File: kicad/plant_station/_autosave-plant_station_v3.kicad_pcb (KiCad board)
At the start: 2 copper layers, 73.4 x 43 mm, 89 parts, among them IC1 VEML7700-TT, IC3 TLC555CDR, IC4 ADC081C021CIMK_NOPB, J1 Conn_02x08_Odd_Even, J10 I2C HOST, J11 SOIL_I2C, J12 WEATHER_I2C, J13 ZF5S-20-01-T-WT-TR, J14 505567-0471, J15 505567-0471, J16 Conn_01x06, J17 Conn_01x08, J18 Conn_01x08, J19 Ammeter_Jumper, J2 MB_I2C, J3 MB_I2C, J4 ZF5S-20-01-T-WT-TR, J5 MB_I2C, J6 MB_I2C, J7 Conn_01x08, J8 Conn_01x06, J9 I2C SCREEN, P1 USB_C_Plug_USB2.0, Q1 DTC113Z, Q3 DTC113Z, Q4 DMG2301L, Q5 BC817DS,115, U1 HDC2010YPAT, U4 ESP-WROOM-02, U5 TPL5110, U6 CP2102N-A01-GQFN28

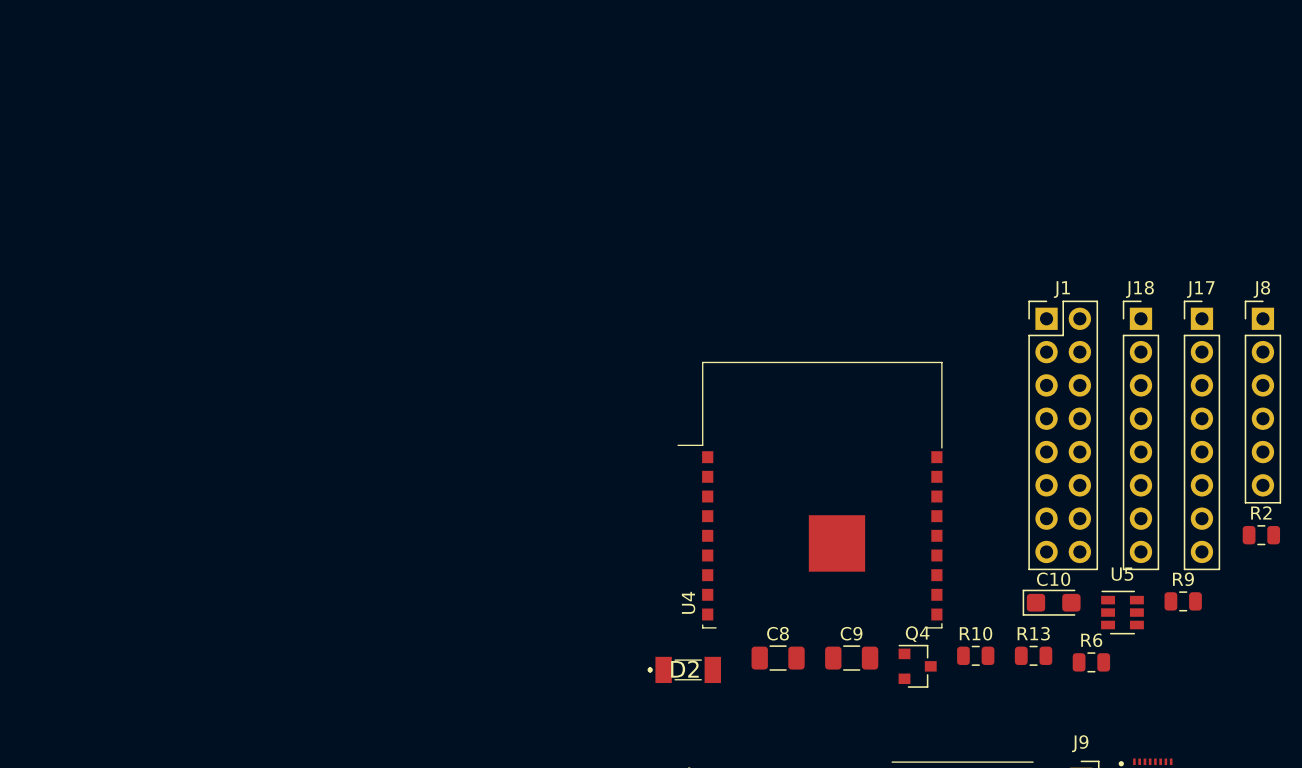
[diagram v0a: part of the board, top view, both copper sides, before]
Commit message: v3 PCB in progress. Need to move LED driver to LEDs board and make it connect using the standard interface
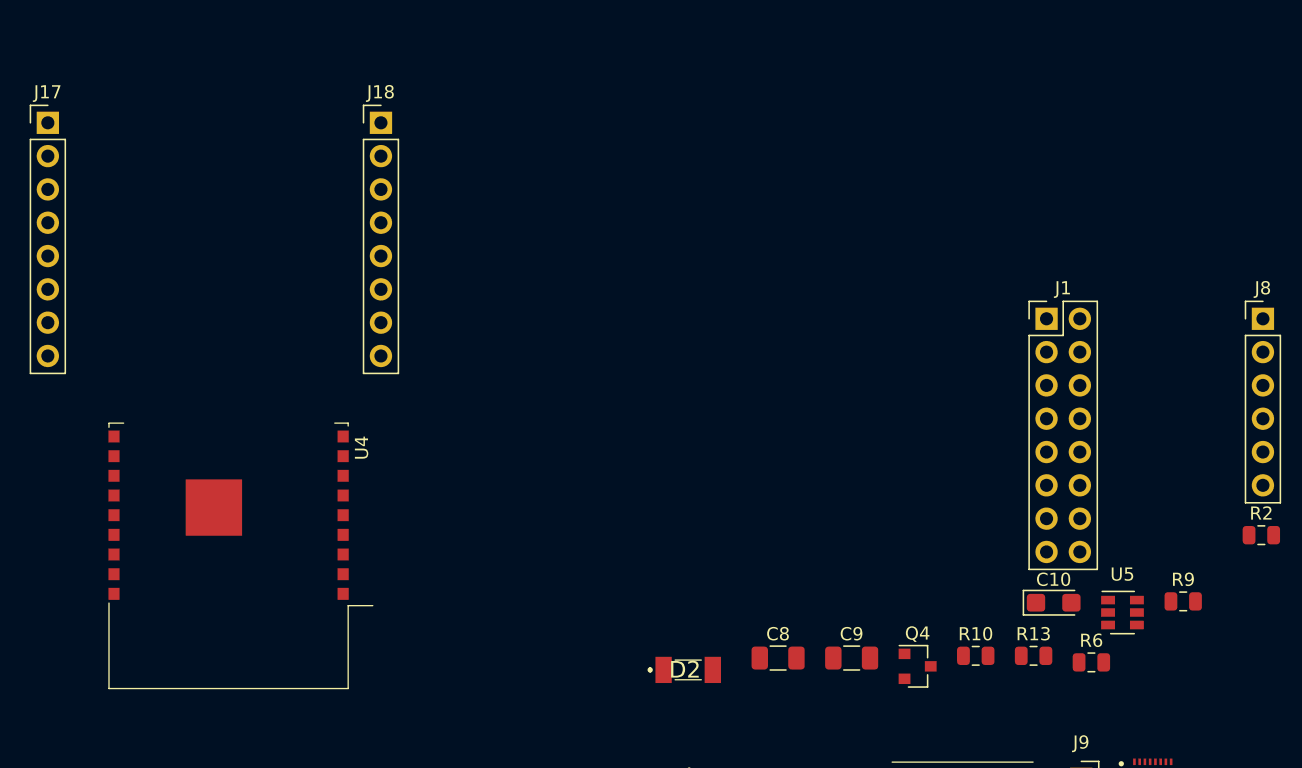
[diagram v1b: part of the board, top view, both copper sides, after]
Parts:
- moved J17 89.3 mm to (45.7, 68.6)
- moved J18 59.9 mm to (71.1, 68.6)
- moved U4 45.3 mm to (59.5, 98.5), turned to 180 degrees
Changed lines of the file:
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@@
   )
   (module Connector_PinHeader_2.54mm:PinHeader_1x08_P2.54mm_Vertical (layer F.Cu)
-    (at 133.725001 83.525001)
+    (at 45.72 68.58)
     (descr "Through hole straight pin header, 1x08, 2.54mm pitch, single row")
     (tags "Through hole pin header THT 1x08 2.54mm single row")
@@
   )
   (module Connector_PinHeader_2.54mm:PinHeader_1x08_P2.54mm_Vertical (layer F.Cu)
-    (at 129.075001 83.525001)
+    (at 71.12 68.58)
     (descr "Through hole straight pin header, 1x08, 2.54mm pitch, single row")
     (tags "Through hole pin header THT 1x08 2.54mm single row")
@@
   )
   (module RF_Module:ESP-WROOM-02 (layer F.Cu)
-    (at 104.775001 100.075001)
+    (at 59.5 98.5 180)
     (descr http://espressif.com/sites/default/files/documentation/0c-esp-wroom-02_datasheet_en.pdf)
     (tags "ESP WROOM-02 espressif esp8266ex")
@@
       (effects (font (size 1 1) (thickness 0.15)))
     )
-    (pad 18 smd rect (at 8.7375 -6) (size 0.85 0.9125) (layers F.Cu F.Paste F.Mask)
-      (net 1 GND))
-    (pad 17 smd rect (at 8.7375 -4.5) (size 0.85 0.9125) (layers F.Cu F.Paste F.Mask)
+    (pad 18 smd rect (at 8.7375 -6 180) (size 0.85 0.9125) (layers F.Cu F.Paste F.Mask)
+      (net 1 GND))
+    (pad 17 smd rect (at 8.7375 -4.5 180) (size 0.85 0.9125) (layers F.Cu F.Paste F.Mask)
       (net 22 /HOST_WAKE))
-    (pad 16 smd rect (at 8.7375 -3) (size 0.85 0.9125) (layers F.Cu F.Paste F.Mask)
+    (pad 16 smd rect (at 8.7375 -3 180) (size 0.85 0.9125) (layers F.Cu F.Paste F.Mask)
       (net 89 "Net-(U4-Pad16)"))
-    (pad 15 smd rect (at 8.7375 -1.5) (size 0.85 0.9125) (layers F.Cu F.Paste F.Mask)
+    (pad 15 smd rect (at 8.7375 -1.5 180) (size 0.85 0.9125) (layers F.Cu F.Paste F.Mask)
       (net 6 /esp8266/ESP_RST))
-    (pad 14 smd rect (at 8.7375 0) (size 0.85 0.9125) (layers F.Cu F.Paste F.Mask)
+    (pad 14 smd rect (at 8.7375 0 180) (size 0.85 0.9125) (layers F.Cu F.Paste F.Mask)
       (net 52 /esp8266/GPIO5))
-    (pad 13 smd rect (at 8.7375 1.5) (size 0.85 0.9125) (layers F.Cu F.Paste F.Mask)
-      (net 1 GND))
-    (pad 12 smd rect (at 8.7375 3) (size 0.85 0.9125) (layers F.Cu F.Paste F.Mask)
+    (pad 13 smd rect (at 8.7375 1.5 180) (size 0.85 0.9125) (layers F.Cu F.Paste F.Mask)
+      (net 1 GND))
+    (pad 12 smd rect (at 8.7375 3 180) (size 0.85 0.9125) (layers F.Cu F.Paste F.Mask)
       (net 55 /esp8266/USB_RXD))
-    (pad 11 smd rect (at 8.7375 4.5) (size 0.85 0.9125) (layers F.Cu F.Paste F.Mask)
+    (pad 11 smd rect (at 8.7375 4.5 180) (size 0.85 0.9125) (layers F.Cu F.Paste F.Mask)
       (net 54 /esp8266/USB_TXD))
-    (pad 10 smd rect (at 8.7375 6) (size 0.85 0.9125) (layers F.Cu F.Paste F.Mask)
+    (pad 10 smd rect (at 8.7375 6 180) (size 0.85 0.9125) (layers F.Cu F.Paste F.Mask)
       (net 11 /ALL_EN))
-    (pad 9 smd rect (at -8.7375 6) (size 0.85 0.9125) (layers F.Cu F.Paste F.Mask)
-      (net 1 GND))
-    (pad 8 smd rect (at -8.7375 4.5) (size 0.85 0.9125) (layers F.Cu F.Paste F.Mask)
+    (pad 9 smd rect (at -8.7375 6 180) (size 0.85 0.9125) (layers F.Cu F.Paste F.Mask)
+      (net 1 GND))
+    (pad 8 smd rect (at -8.7375 4.5 180) (size 0.85 0.9125) (layers F.Cu F.Paste F.Mask)
       (net 53 /esp8266/GPIO0))
-    (pad 7 smd rect (at -8.7375 3) (size 0.85 0.9125) (layers F.Cu F.Paste F.Mask)
+    (pad 7 smd rect (at -8.7375 3 180) (size 0.85 0.9125) (layers F.Cu F.Paste F.Mask)
       (net 20 /SDA))
-    (pad 6 smd rect (at -8.7375 1.5) (size 0.85 0.9125) (layers F.Cu F.Paste F.Mask)
+    (pad 6 smd rect (at -8.7375 1.5 180) (size 0.85 0.9125) (layers F.Cu F.Paste F.Mask)
       (net 49 /esp8266/GPIO15))
-    (pad 5 smd rect (at -8.7375 0) (size 0.85 0.9125) (layers F.Cu F.Paste F.Mask)
+    (pad 5 smd rect (at -8.7375 0 180) (size 0.85 0.9125) (layers F.Cu F.Paste F.Mask)
       (net 50 /esp8266/GPIO13))
-    (pad 4 smd rect (at -8.7375 -1.5) (size 0.85 0.9125) (layers F.Cu F.Paste F.Mask)
+    (pad 4 smd rect (at -8.7375 -1.5 180) (size 0.85 0.9125) (layers F.Cu F.Paste F.Mask)
       (net 51 /esp8266/GPIO12))
-    (pad 3 smd rect (at -8.7375 -3) (size 0.85 0.9125) (layers F.Cu F.Paste F.Mask)
+    (pad 3 smd rect (at -8.7375 -3 180) (size 0.85 0.9125) (layers F.Cu F.Paste F.Mask)
       (net 21 /SCL))
-    (pad 2 smd rect (at -8.7375 -4.5) (size 0.85 0.9125) (layers F.Cu F.Paste F.Mask)
+    (pad 2 smd rect (at -8.7375 -4.5 180) (size 0.85 0.9125) (layers F.Cu F.Paste F.Mask)
       (net 7 /esp8266/ESP_EN))
-    (pad 1 smd rect (at -8.7375 -6) (size 0.85 0.9125) (layers F.Cu F.Paste F.Mask)
+    (pad 1 smd rect (at -8.7375 -6 180) (size 0.85 0.9125) (layers F.Cu F.Paste F.Mask)
       (net 3 +3V3))
-    (pad 19 smd rect (at 1.12 0.58) (size 4.3 4.3) (layers F.Cu F.Paste F.Mask)
+    (pad 19 smd rect (at 1.12 0.58 180) (size 4.3 4.3) (layers F.Cu F.Paste F.Mask)
       (net 1 GND))
     (model ${KISYS3DMOD}/RF_Module.3dshapes/ESP-WROOM-02.wrl
